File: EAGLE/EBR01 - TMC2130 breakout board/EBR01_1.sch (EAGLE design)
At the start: 24 parts, among them J1 CPL-CON-HEADER-0.1IN-8P-M, J2 CPL-CON-HEADER-0.1IN-8P-M, J3 CPL-CON-HEADER-0.1IN-2X3P-M, U2 CPL-REG-LIN-5V-0.1A

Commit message: Schematic tentative finalized.
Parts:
- removed C14, C15: 100nF, TinWhiskers:CPL-CAP-X7R-0603-100NF-50V
- removed R3: 0.22, TinWhiskers:CPL-RES-1206-0.22-0.5W
- added C2: 0.33uF, TinWhiskers:CPL-CAP-X7R-0603-0.33UF-35V
- added C3: 100 nF, TinWhiskers:CPL-CAP-X7R-0603-100NF-50V
- added R1: 0.22, TinWhiskers:CPL-RES-1206-0.22-0.5W
- C12, C13: value 470pF -> 100nF; device TinWhiskers:CPL-CAP-X7R-0603-470PF-100V -> TinWhiskers:CPL-CAP-X7R-0603-100NF-50V
- C4: value 0.1uF -> 100 nF; device TinWhiskers:CPL-CAP-X7R-0603-0.1UF-35V -> TinWhiskers:CPL-CAP-X7R-0603-100NF-50V
- C5: value 0.33uF -> 22 nF; device TinWhiskers:CPL-CAP-X7R-0603-0.33UF-35V -> TinWhiskers:CPL-CAP-X7R-0603-22NF-50V"
- C7: value 22 nF -> 100 nF; device TinWhiskers:CPL-CAP-X7R-0603-22NF-50V" -> TinWhiskers:CPL-CAP-X7R-0603-100NF-50V
- C8, C9: value 100 nF -> 470pF; device TinWhiskers:CPL-CAP-X7R-0603-100NF-50V -> TinWhiskers:CPL-CAP-X7R-0603-470PF-100V
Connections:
- net 1A: now also C10.1; no longer C12.1
- net 1B: now also C11.1; no longer C13.1
- net 2A: now also C9.1; no longer C11.1
- net 2B: now also C8.1; no longer C10.1
- net GND: now also C2.1, C3.1, C6.2, C7.2, R1.1; no longer C14.2, C15.2, C4.1, C5.1, R3.1
- net N$1: now also C5.2; no longer C7.2
- net N$3: now also C12.1, R1.2; no longer C14.1, R2.2
- net N$4: now also C13.1, R2.2; no longer C15.1, R3.2
- net N$5: now also C5.1; no longer C7.1
- net N$8: now also C4.1; no longer C6.1
- net VCC: now also C3.2; no longer C4.2
- net VMOT: now also C2.2, C4.2, C6.1, C7.1; no longer C5.2, C6.2, C8.1, C9.1
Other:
- moved on the sheet: C10, C11, C6, C7, R2

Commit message: Breakout board layout
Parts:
- U1: value (none) -> TMC2130-LA
- renumbered U2 to Q1

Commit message: Corrected all (118) DRC errors for EBR01 board. Thickened traces for R2 GND connection, added extra vias to improve grounding, rerouted N$3 trace running directly under GND pad so more vias could be added for improved thermal protection. General tuneups of the traces were done. Corrected some of the nomenclature on the schematic to provide more detailed information.
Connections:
- net N$4 renamed BRB
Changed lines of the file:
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@@
 </segment>
 </net>
-<net name="N$4" class="0">
+<net name="BRB" class="0">
 <segment>
 <pinref part="D3" gate="G$1" pin="A"/>

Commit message: Added vias to R1 GND connection, made all traces to GND wider. Moved board up so that Y=0 lines up with the bottom of the board and fixed Y dimension to reflect true height. Overall cleanup of vias and location.
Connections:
- net N$3 renamed BRA
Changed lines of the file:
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@@
 </segment>
 </net>
-<net name="N$3" class="0">
+<net name="BRA" class="0">
 <segment>
 <pinref part="D1" gate="G$1" pin="A"/>

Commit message: Tweaked routing and placement on board.  This is the version that will be submitted to the board house.  Exported GERBERs and checked them in.
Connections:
- net N$1 renamed CPI
- net N$5 renamed CPO
- net N$8 renamed VCP
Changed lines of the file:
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@@
 </segment>
 </net>
-<net name="N$1" class="0">
+<net name="CPI" class="0">
 <segment>
 <wire x1="210.82" y1="165.1" x2="205.74" y2="165.1" width="0.1524" layer="91"/>
@@
 </segment>
 </net>
-<net name="N$5" class="0">
+<net name="CPO" class="0">
 <segment>
 <pinref part="U1" gate="G$1" pin="CPO"/>
@@
 </segment>
 </net>
-<net name="N$8" class="0">
+<net name="VCP" class="0">
 <segment>
 <pinref part="U1" gate="G$1" pin="VCP"/>

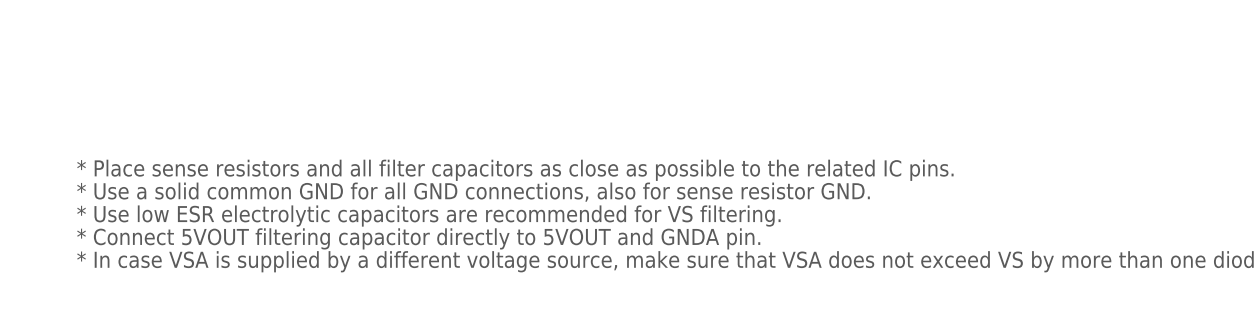
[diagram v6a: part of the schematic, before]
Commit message: Updated schematic to include UART0, UART1, MicroSD, SWD, RS-485.
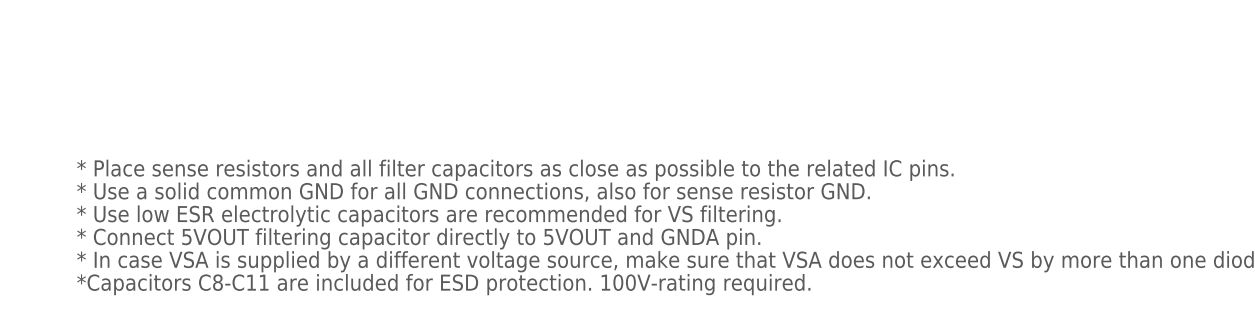
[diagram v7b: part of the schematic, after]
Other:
- note added: "*Capacitors C8-C11 are included for ESD protection. 100V-rating required."
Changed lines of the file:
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@@
 <text x="147.32" y="132.08" size="1.778" layer="97">N/C</text>
 <text x="33.02" y="180.34" size="1.778" layer="97">Linear Regulator Circuit</text>
+<text x="30.48" y="43.18" size="1.778" layer="97">*Capacitors C8-C11 are included for ESD protection. 100V-rating required.</text>
 </plain>
 <instances>

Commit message: Integrated motor drivers into the EMC03 schematic, E-checked the EBR01 board with the netlist. Began similarifying things cromulently.
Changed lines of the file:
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@@
 <?xml version="1.0" encoding="utf-8"?>
 <!DOCTYPE eagle SYSTEM "eagle.dtd">
-<eagle version="7.3.0">
+<eagle version="7.4.0">
 <drawing>
 <settings>
@@
 <wire x1="38.1" y1="172.72" x2="35.56" y2="172.72" width="0.1524" layer="91"/>
 <junction x="38.1" y="172.72"/>
-<label x="35.56" y="172.72" size="1.778" layer="95" rot="R180" xref="yes"/>
+<label x="33.02" y="172.72" size="1.778" layer="95"/>
 </segment>
 </net>
@@
 <wire x1="149.86" y1="175.26" x2="149.86" y2="172.72" width="0.1524" layer="91"/>
 <junction x="149.86" y="172.72"/>
-<label x="142.24" y="172.72" size="1.778" layer="95" rot="R180" xref="yes"/>
+<label x="139.7" y="172.72" size="1.778" layer="95"/>
 </segment>
 <segment>
@@
 <junction x="63.5" y="172.72"/>
 <pinref part="C3" gate="C1" pin="2"/>
-<label x="66.04" y="172.72" size="1.778" layer="95" xref="yes"/>
-</segment>
-</net>
+<label x="66.04" y="172.72" size="1.778" layer="95"/>
+</segment>
+</net>
